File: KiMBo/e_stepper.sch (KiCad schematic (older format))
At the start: 24 parts, among them U21 TMC2130

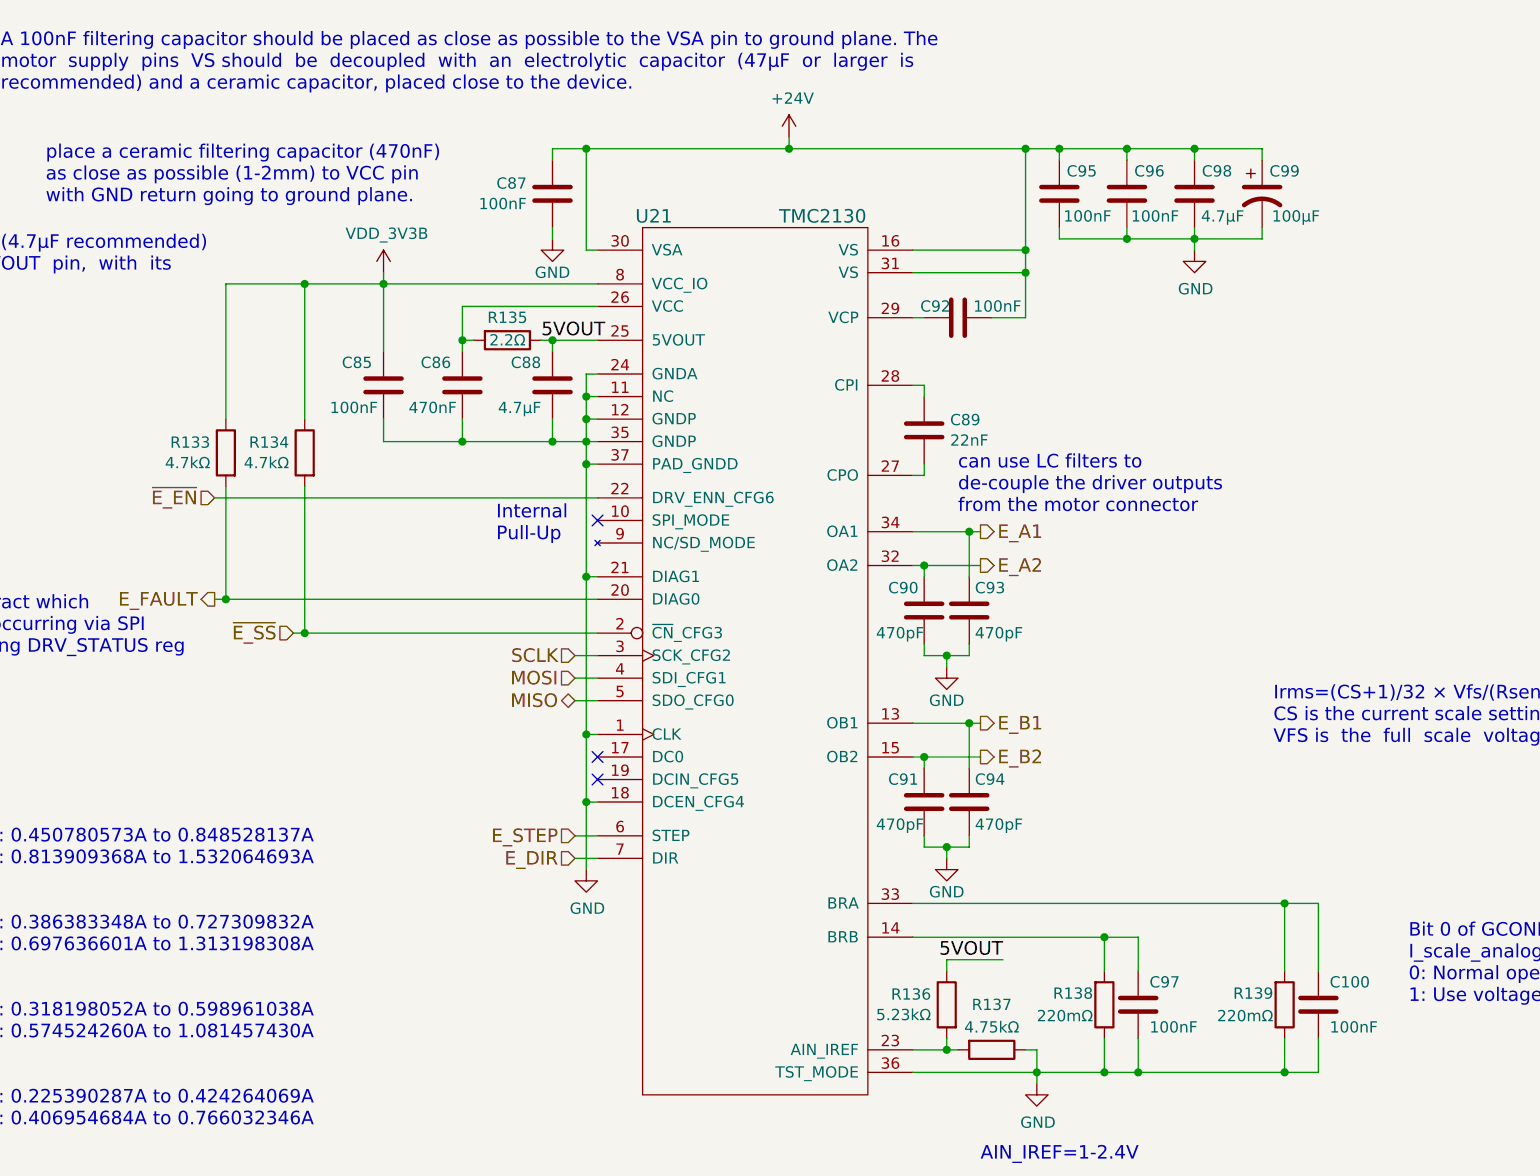
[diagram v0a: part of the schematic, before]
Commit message: Add equivalent annotations document, associate more footprints
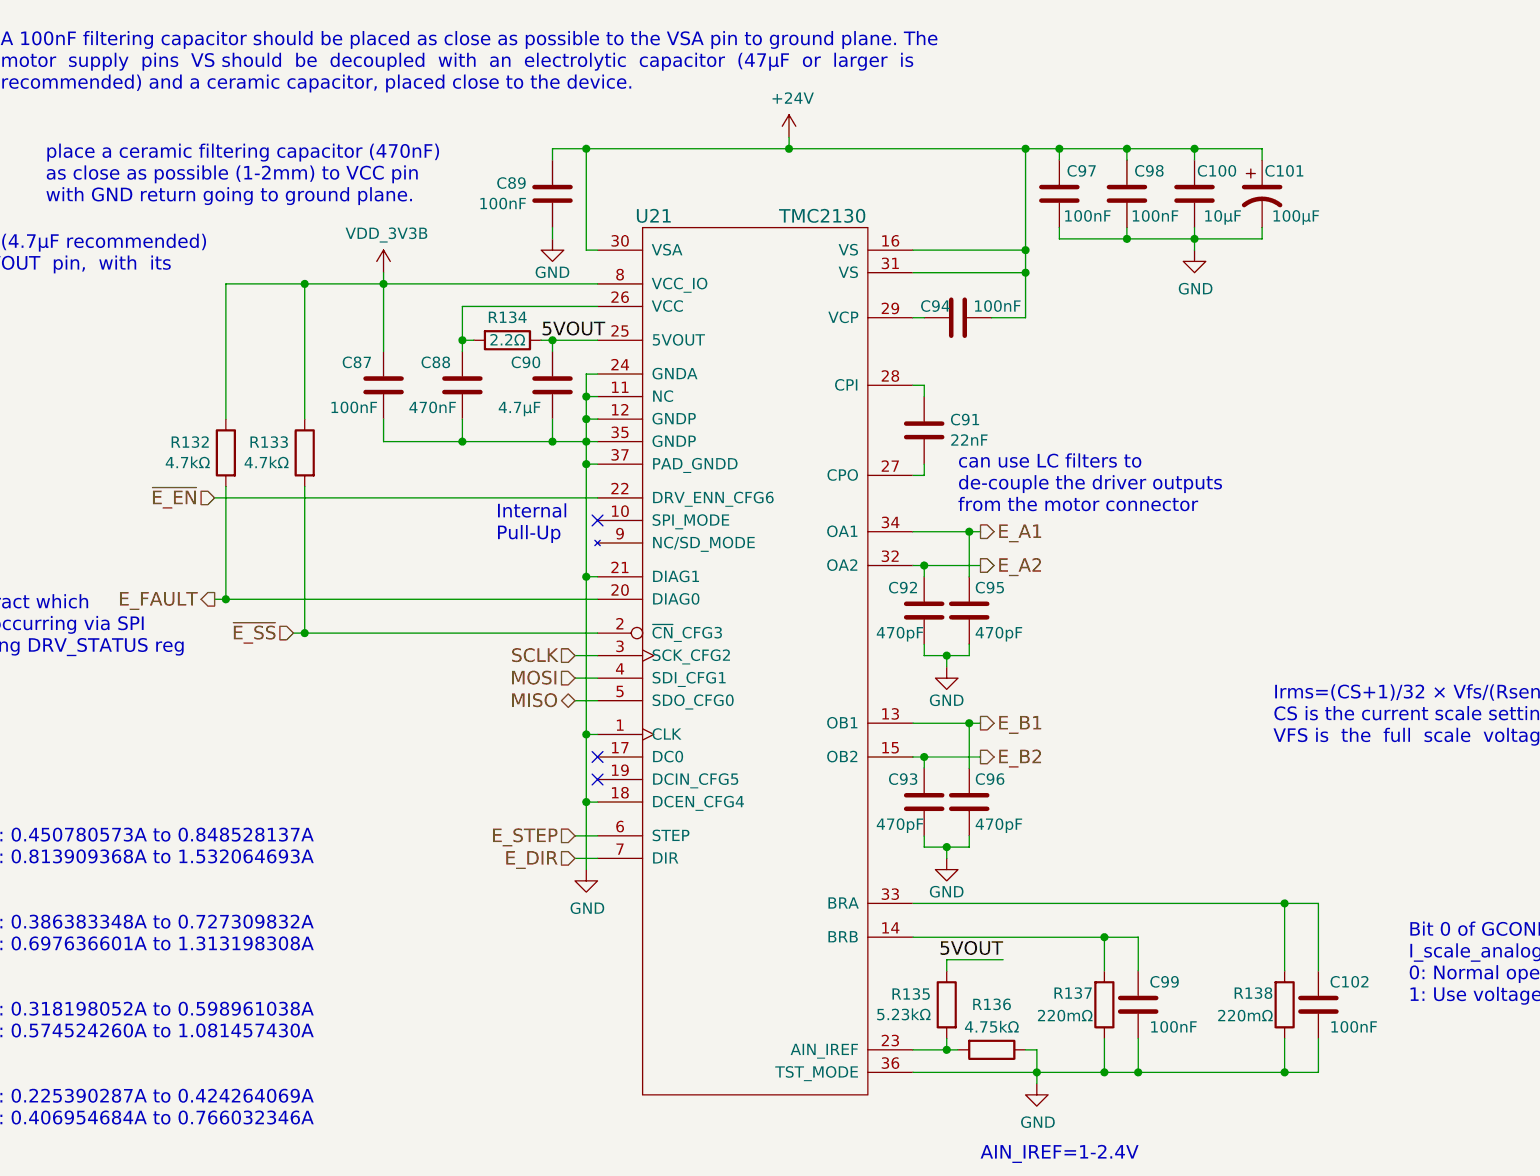
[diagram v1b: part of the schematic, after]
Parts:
- C100: renamed from C98; value 4.7μF -> 10μF; footprint (none) -> Capacitors_SMD:C_0805
- C101: renamed from C99; footprint (none) -> Capacitors_SMD:c_elec_8x10
- C102: renamed from C100; footprint (none) -> Capacitors_SMD:C_0603
- C87: renamed from C85; footprint (none) -> Capacitors_SMD:C_0603
- C88: renamed from C86; footprint (none) -> Capacitors_SMD:C_0603
- C89: renamed from C87; footprint (none) -> Capacitors_SMD:C_0603
- C90: renamed from C88; footprint (none) -> Capacitors_SMD:C_0402
- C91: renamed from C89; footprint (none) -> Capacitors_SMD:C_0402
- C92: renamed from C90; footprint (none) -> Capacitors_SMD:C_0603
- C93: renamed from C91; footprint (none) -> Capacitors_SMD:C_0603
- C94: renamed from C92; footprint (none) -> Capacitors_SMD:C_0603
- C95: renamed from C93; footprint (none) -> Capacitors_SMD:C_0603
- C96: renamed from C94; footprint (none) -> Capacitors_SMD:C_0603
- C97: renamed from C95; footprint (none) -> Capacitors_SMD:C_0603
- C98: renamed from C96; footprint (none) -> Capacitors_SMD:C_0603
- C99: renamed from C97; footprint (none) -> Capacitors_SMD:C_0603
- renumbered R133 to R132, R134 to R133, R135 to R134, R136 to R135, R137 to R136, R138 to R137, R139 to R138
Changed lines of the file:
@@
 MOSI
 $Comp
-L C C87
+L C C89
 U 1 1 589B8A74
 P 7300 3950
-F 0 "C87" H 7186 3904 50  0000 R CNN
+F 0 "C89" H 7186 3904 50  0000 R CNN
 F 1 "100nF" H 7186 3995 50  0000 R CNN
-F 2 "" H 7338 3800 50  0001 C CNN
+F 2 "Capacitors_SMD:C_0603" H 7338 3800 50  0001 C CNN
 F 3 "" H 7300 3950 50  0000 C CNN
 	1    7300 3950
@@
 $EndComp
 $Comp
-L C C92
+L C C94
 U 1 1 5BA7E11F
 P 9100 4500
-F 0 "C92" V 9050 4400 50  0000 C CNN
+F 0 "C94" V 9050 4400 50  0000 C CNN
 F 1 "100nF" V 9050 4675 50  0000 C CNN
-F 2 "" H 9138 4350 50  0001 C CNN
+F 2 "Capacitors_SMD:C_0603" H 9138 4350 50  0001 C CNN
 F 3 "" H 9100 4500 50  0000 C CNN
 	1    9100 4500
@@
 $EndComp
 $Comp
-L CP1 C99
+L CP1 C101
 U 1 1 5BA7E120
 P 10450 3950
-F 0 "C99" H 10550 4050 50  0000 C CNN
+F 0 "C101" H 10550 4050 50  0000 C CNN
 F 1 "100μF" H 10600 3850 50  0000 C CNN
-F 2 "" H 10450 3950 50  0001 C CNN
+F 2 "Capacitors_SMD:c_elec_8x10" H 10450 3950 50  0001 C CNN
 F 3 "" H 10450 3950 50  0000 C CNN
 	1    10450 3950
@@
 $EndComp
 $Comp
-L C C95
+L C C97
 U 1 1 589BC941
 P 9550 3950
-F 0 "C95" H 9450 4050 50  0000 C CNN
+F 0 "C97" H 9450 4050 50  0000 C CNN
 F 1 "100nF" H 9425 3850 50  0000 C CNN
-F 2 "" H 9588 3800 50  0001 C CNN
+F 2 "Capacitors_SMD:C_0603" H 9588 3800 50  0001 C CNN
 F 3 "" H 9550 3950 50  0000 C CNN
 	1    9550 3950
@@
 $EndComp
 $Comp
-L GND #PWR0209
+L GND #PWR0210
 U 1 1 589BD203
 P 7300 4150
-F 0 "#PWR0209" H 7300 3900 50  0001 C CNN
+F 0 "#PWR0210" H 7300 3900 50  0001 C CNN
 F 1 "GND" H 7300 4000 50  0000 C CNN
 F 2 "" H 7300 4150 50  0000 C CNN
@@
 $EndComp
 $Comp
-L C C96
+L C C98
 U 1 1 589BDAA2
 P 9850 3950
-F 0 "C96" H 9750 4050 50  0000 C CNN
+F 0 "C98" H 9750 4050 50  0000 C CNN
 F 1 "100nF" H 9725 3850 50  0000 C CNN
-F 2 "" H 9888 3800 50  0001 C CNN
+F 2 "Capacitors_SMD:C_0603" H 9888 3800 50  0001 C CNN
 F 3 "" H 9850 3950 50  0000 C CNN
 	1    9850 3950
@@
 $EndComp
 $Comp
-L GND #PWR0210
+L GND #PWR0211
 U 1 1 589BE47E
 P 10150 4200
-F 0 "#PWR0210" H 10150 3950 50  0001 C CNN
+F 0 "#PWR0211" H 10150 3950 50  0001 C CNN
 F 1 "GND" H 10155 4027 50  0000 C CNN
 F 2 "" H 10150 4200 50  0000 C CNN
@@
 $EndComp
 $Comp
-L +24V #PWR0211
+L +24V #PWR0212
 U 1 1 5BA7E125
 P 8350 3700
-F 0 "#PWR0211" H 8350 3550 50  0001 C CNN
+F 0 "#PWR0212" H 8350 3550 50  0001 C CNN
 F 1 "+24V" H 8365 3873 50  0000 C CNN
 F 2 "" H 8350 3700 50  0000 C CNN
@@
 $EndComp
 $Comp
-L C C89
+L C C91
 U 1 1 589C0BAD
 P 8950 5000
-F 0 "C89" H 9065 5046 50  0000 L CNN
+F 0 "C91" H 9065 5046 50  0000 L CNN
 F 1 "22nF" H 9065 4955 50  0000 L CNN
-F 2 "" H 8988 4850 50  0001 C CNN
+F 2 "Capacitors_SMD:C_0402" H 8988 4850 50  0001 C CNN
 F 3 "" H 8950 5000 50  0000 C CNN
 	1    8950 5000
@@
 $EndComp
 $Comp
-L R R139
+L R R138
 U 1 1 589C1BED
 P 10550 7550
-F 0 "R139" H 10500 7500 50  0000 R CNN
+F 0 "R138" H 10500 7500 50  0000 R CNN
 F 1 "220mΩ" H 10500 7600 50  0000 R CNN
 F 2 "" V 10480 7550 50  0001 C CNN
@@
 $EndComp
 $Comp
-L R R138
+L R R137
 U 1 1 589C1CA7
 P 9750 7550
-F 0 "R138" H 9700 7500 50  0000 R CNN
+F 0 "R137" H 9700 7500 50  0000 R CNN
 F 1 "220mΩ" H 9700 7600 50  0000 R CNN
 F 2 "" V 9680 7550 50  0001 C CNN
@@
 $EndComp
 $Comp
-L GND #PWR0212
+L GND #PWR0213
 U 1 1 5BA7E129
 P 9450 7900
-F 0 "#PWR0212" H 9450 7650 50  0001 C CNN
+F 0 "#PWR0213" H 9450 7650 50  0001 C CNN
 F 1 "GND" H 9455 7727 50  0000 C CNN
 F 2 "" H 9450 7900 50  0000 C CNN
@@
 NoConn ~ 7500 6450
 $Comp
-L R R135
+L R R134
 U 1 1 5BA7E12B
 P 7100 4600
-F 0 "R135" V 7000 4600 50  0000 C CNN
+F 0 "R134" V 7000 4600 50  0000 C CNN
 F 1 "2.2Ω" V 7100 4600 50  0000 C CNN
 F 2 "" V 7030 4600 50  0001 C CNN
@@
 $EndComp
 $Comp
-L C C86
+L C C88
 U 1 1 589C52DF
 P 6900 4800
-F 0 "C86" H 6950 4900 50  0000 L CNN
+F 0 "C88" H 6950 4900 50  0000 L CNN
 F 1 "470nF" H 6925 4700 50  0000 L CNN
-F 2 "" H 6938 4650 50  0001 C CNN
+F 2 "Capacitors_SMD:C_0603" H 6938 4650 50  0001 C CNN
 F 3 "" H 6900 4800 50  0000 C CNN
 	1    6900 4800
@@
 NoConn ~ 7500 6550
 $Comp
-L GND #PWR0213
+L GND #PWR0214
 U 1 1 589C97FF
 P 7450 6950
-F 0 "#PWR0213" H 7450 6700 50  0001 C CNN
+F 0 "#PWR0214" H 7450 6700 50  0001 C CNN
 F 1 "GND" H 7455 6777 50  0000 C CNN
 F 2 "" H 7450 6950 50  0000 C CNN
@@
 $EndComp
 $Comp
-L C C97
+L C C99
 U 1 1 5BA7E12E
 P 9900 7550
-F 0 "C97" H 9950 7650 50  0000 L CNN
+F 0 "C99" H 9950 7650 50  0000 L CNN
 F 1 "100nF" H 9950 7450 50  0000 L CNN
-F 2 "" H 9938 7400 50  0001 C CNN
+F 2 "Capacitors_SMD:C_0603" H 9938 7400 50  0001 C CNN
 F 3 "" H 9900 7550 50  0000 C CNN
 	1    9900 7550
@@
 E_FAULT
 $Comp
-L R R133
+L R R132
 U 1 1 589D21BC
 P 5850 5100
-F 0 "R133" H 5919 5146 50  0000 L CNN
+F 0 "R132" H 5919 5146 50  0000 L CNN
 F 1 "4.7kΩ" H 5919 5055 50  0000 L CNN
 F 2 "" V 5780 5100 50  0001 C CNN
@@
 Internal\nPull-Up
 $Comp
-L C C88
+L C C90
 U 1 1 5BA7E12A
 P 7300 4800
-F 0 "C88" H 7350 4900 50  0000 L CNN
+F 0 "C90" H 7350 4900 50  0000 L CNN
 F 1 "4.7μF" H 7350 4700 50  0000 L CNN
-F 2 "" H 7338 4650 50  0001 C CNN
+F 2 "Capacitors_SMD:C_0402" H 7338 4650 50  0001 C CNN
 F 3 "" H 7300 4800 50  0000 C CNN
 	1    7300 4800
@@
 5VOUT
 $Comp
-L R R136
+L R R135
 U 1 1 589E13FD
 P 9050 7550
-F 0 "R136" H 9119 7596 50  0000 L CNN
+F 0 "R135" H 9119 7596 50  0000 L CNN
 F 1 "5.23kΩ" H 9119 7505 50  0000 L CNN
 F 2 "" V 8980 7550 50  0001 C CNN
@@
 5VOUT
 $Comp
-L R R137
+L R R136
 U 1 1 589E24D4
 P 9250 7750
-F 0 "R137" V 9050 7750 50  0000 C CNN
+F 0 "R136" V 9050 7750 50  0000 C CNN
 F 1 "4.75kΩ" V 9150 7750 50  0000 C CNN
 F 2 "" V 9180 7750 50  0001 C CNN
@@
 AIN_IREF=1-2.4V
 $Comp
-L R R134
+L R R133
 U 1 1 5BA7E132
 P 6200 5100
-F 0 "R134" H 6269 5146 50  0000 L CNN
+F 0 "R133" H 6269 5146 50  0000 L CNN
 F 1 "4.7kΩ" H 6269 5055 50  0000 L CNN
 F 2 "" V 6130 5100 50  0001 C CNN
@@
 $EndComp
 $Comp
-L C C100
+L C C102
 U 1 1 5BA7E133
 P 10700 7550
-F 0 "C100" H 10750 7650 50  0000 L CNN
+F 0 "C102" H 10750 7650 50  0000 L CNN
 F 1 "100nF" H 10750 7450 50  0000 L CNN
-F 2 "" H 10738 7400 50  0001 C CNN
+F 2 "Capacitors_SMD:C_0603" H 10738 7400 50  0001 C CNN
 F 3 "" H 10700 7550 50  0000 C CNN
 	1    10700 7550
@@
 Choose  sense  resistors  in  a  way,  that  normal \nIRUN is 16 to 31 for best microstep performance.
 $Comp
-L C C90
+L C C92
 U 1 1 5BA7E134
 P 8950 5800
-F 0 "C90" H 8975 5900 50  0000 L CNN
+F 0 "C92" H 8975 5900 50  0000 L CNN
 F 1 "470pF" H 8950 5700 50  0000 L CNN
-F 2 "" H 8988 5650 50  0001 C CNN
+F 2 "Capacitors_SMD:C_0603" H 8988 5650 50  0001 C CNN
 F 3 "" H 8950 5800 50  0000 C CNN
 	1    8950 5800
@@
 $EndComp
 $Comp
-L GND #PWR0214
+L GND #PWR0215
 U 1 1 58B19D33
 P 9050 6050
-F 0 "#PWR0214" H 9050 5800 50  0001 C CNN
+F 0 "#PWR0215" H 9050 5800 50  0001 C CNN
 F 1 "GND" H 9050 5900 50  0000 C CNN
 F 2 "" H 9050 6050 50  0000 C CNN
@@
 $EndComp
 $Comp
-L C C93
+L C C95
 U 1 1 58B1B794
 P 9150 5800
-F 0 "C93" H 9175 5900 50  0000 L CNN
+F 0 "C95" H 9175 5900 50  0000 L CNN
 F 1 "470pF" H 9175 5700 50  0000 L CNN
-F 2 "" H 9188 5650 50  0001 C CNN
+F 2 "Capacitors_SMD:C_0603" H 9188 5650 50  0001 C CNN
 F 3 "" H 9150 5800 50  0000 C CNN
 	1    9150 5800
@@
 $EndComp
 $Comp
-L C C91
+L C C93
 U 1 1 58B1C6FD
 P 8950 6650
-F 0 "C91" H 8975 6750 50  0000 L CNN
+F 0 "C93" H 8975 6750 50  0000 L CNN
 F 1 "470pF" H 8950 6550 50  0000 L CNN
-F 2 "" H 8988 6500 50  0001 C CNN
+F 2 "Capacitors_SMD:C_0603" H 8988 6500 50  0001 C CNN
 F 3 "" H 8950 6650 50  0000 C CNN
 	1    8950 6650
@@
 $EndComp
 $Comp
-L GND #PWR0215
+L GND #PWR0216
 U 1 1 58B1C704
 P 9050 6900
-F 0 "#PWR0215" H 9050 6650 50  0001 C CNN
+F 0 "#PWR0216" H 9050 6650 50  0001 C CNN
 F 1 "GND" H 9050 6750 50  0000 C CNN
 F 2 "" H 9050 6900 50  0000 C CNN
@@
 $EndComp
 $Comp
-L C C94
+L C C96
 U 1 1 58B1C710
 P 9150 6650
-F 0 "C94" H 9175 6750 50  0000 L CNN
+F 0 "C96" H 9175 6750 50  0000 L CNN
 F 1 "470pF" H 9175 6550 50  0000 L CNN
-F 2 "" H 9188 6500 50  0001 C CNN
+F 2 "Capacitors_SMD:C_0603" H 9188 6500 50  0001 C CNN
 F 3 "" H 9150 6650 50  0000 C CNN
 	1    9150 6650
@@
 $EndComp
 $Comp
-L C C98
+L C C100
 U 1 1 58B40194
 P 10150 3950
-F 0 "C98" H 10050 4050 50  0000 C CNN
-F 1 "4.7μF" H 10025 3850 50  0000 C CNN
-F 2 "" H 10188 3800 50  0001 C CNN
+F 0 "C100" H 10050 4050 50  0000 C CNN
+F 1 "10μF" H 10025 3850 50  0000 C CNN
+F 2 "Capacitors_SMD:C_0805" H 10188 3800 50  0001 C CNN
 F 3 "" H 10150 3950 50  0000 C CNN
 	1    10150 3950
@@
 Can extract which\nfault is occurring via SPI\nby reading DRV_STATUS reg
 $Comp
-L VDD_3V3B #PWR0216
+L VDD_3V3B #PWR0217
 U 1 1 5A2FD350
 P 6550 4300
-F 0 "#PWR0216" H 6550 4150 50  0001 C CNN
+F 0 "#PWR0217" H 6550 4150 50  0001 C CNN
 F 1 "VDD_3V3B" H 6565 4473 50  0000 C CNN
 F 2 "" H 6550 4300 50  0000 C CNN
@@
 $EndComp
 $Comp
-L C C85
+L C C87
 U 1 1 5A896678
 P 6550 4800
-F 0 "C85" H 6600 4900 50  0000 L CNN
+F 0 "C87" H 6600 4900 50  0000 L CNN
 F 1 "100nF" H 6575 4700 50  0000 L CNN
-F 2 "" H 6588 4650 50  0001 C CNN
+F 2 "Capacitors_SMD:C_0603" H 6588 4650 50  0001 C CNN
 F 3 "" H 6550 4800 50  0000 C CNN
 	1    6550 4800
